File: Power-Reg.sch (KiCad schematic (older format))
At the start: 9 parts, among them U201 MCP6002, U401 TPS7A2401

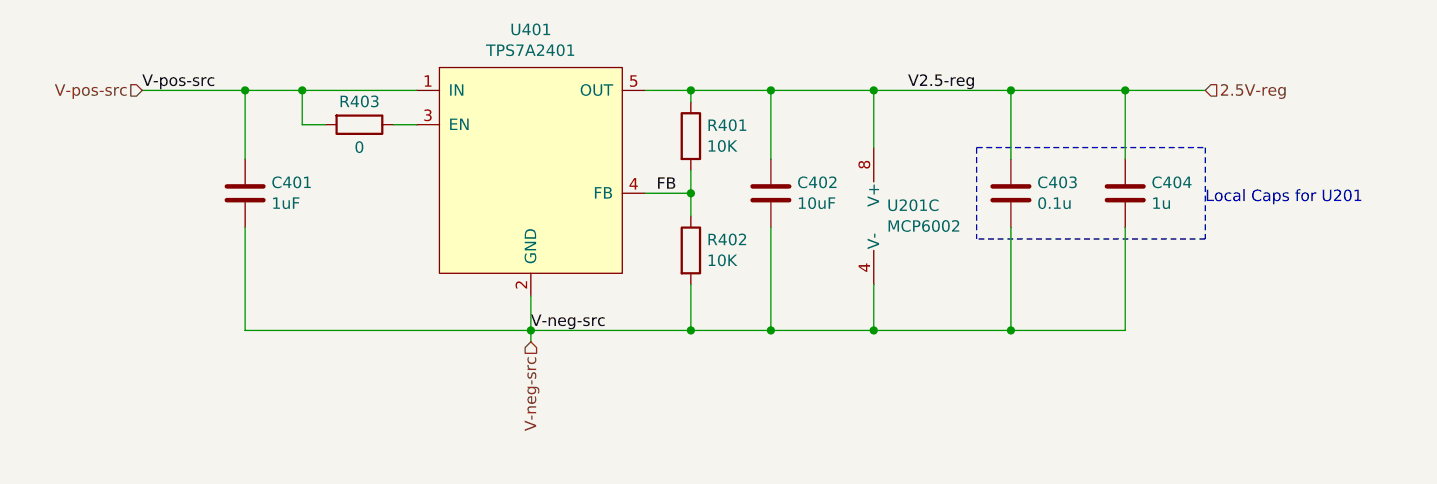
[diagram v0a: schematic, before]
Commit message: PCB completed with Op-Amp mounted horizontally
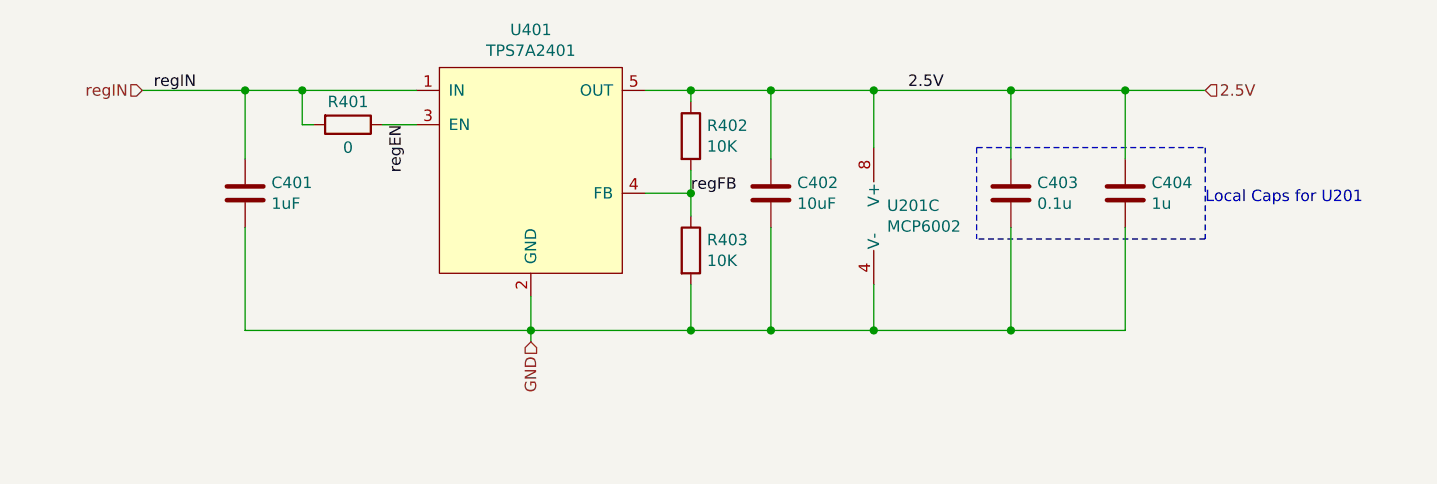
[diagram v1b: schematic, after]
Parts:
- U201: MPN (none) -> MCP6002T-I/SN
- U401: MPN (none) -> TPS7A2401DBVR
- renumbered R403 to R401, R401 to R402, R402 to R403
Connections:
- net regEN: now reaches R401.1, U401.3 (EN)
- net 2.5V-reg renamed 2.5V
- net FB renamed regFB
- net V-neg-src renamed GND
- net V-pos-src renamed regIN
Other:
- moved on the sheet: R401
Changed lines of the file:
@@
 F 2 "Package_SO:SOIC-8_3.9x4.9mm_P1.27mm" H 6950 3800 50  0001 C CNN
 F 3 "http://ww1.microchip.com/downloads/en/DeviceDoc/21733j.pdf" H 6950 3800 50  0001 C CNN
+F 4 "MCP6002T-I/SN" H 6950 3800 50  0001 C CNN "MPN"
 	3    6950 3800
 	1    0    0    -1
@@
 F 1 "TPS7A2401" H 5350 4124 50  0000 C CNN
 F 2 "Package_TO_SOT_SMD:SOT-23-5_HandSoldering" H 5350 3600 50  0001 C CNN
-F 3 "" H 5350 3600 50  0001 C CNN
+F 3 "https://www.ti.com/lit/ds/symlink/tps7a24.pdf?HQS=dis-dk-null-digikeymode-dsf-pf-null-wwe&ts=1613174744075" H 5350 3600 50  0001 C CNN
+F 4 "TPS7A2401DBVR" H 5350 3600 50  0001 C CNN "MPN"
 	1    5350 3600
 	1    0    0    -1
@@
 P 6050 3450
 AR Path="/60164E14" Ref="R?"  Part="1"
-AR Path="/601B7636/60164E14" Ref="R401"  Part="1"
-F 0 "R401" H 6120 3496 50  0000 L CNN
+AR Path="/601B7636/60164E14" Ref="R402"  Part="1"
+F 0 "R402" H 6120 3496 50  0000 L CNN
 F 1 "10K" H 6120 3405 50  0000 L CNN
 F 2 "Resistor_SMD:R_0805_2012Metric_Pad1.20x1.40mm_HandSolder" V 5980 3450 50  0001 C CNN
@@
 P 6050 3950
 AR Path="/60164E1A" Ref="R?"  Part="1"
-AR Path="/601B7636/60164E1A" Ref="R402"  Part="1"
-F 0 "R402" H 6120 3996 50  0000 L CNN
+AR Path="/601B7636/60164E1A" Ref="R403"  Part="1"
+F 0 "R403" H 6120 3996 50  0000 L CNN
 F 1 "10K" H 6120 3905 50  0000 L CNN
 F 2 "Resistor_SMD:R_0805_2012Metric_Pad1.20x1.40mm_HandSolder" V 5980 3950 50  0001 C CNN
@@
 	6400 4300 6050 4300
 Text HLabel 8300 3250 2    50   Input ~ 0
-2.5V-reg
+2.5V
 Wire Wire Line
 	4100 3250 3650 3250
 Connection ~ 4100 3250
-Text HLabel 5350 4350 3    50   Input ~ 0
-V-neg-src
 Text HLabel 3650 3250 0    50   Input ~ 0
-V-pos-src
-Text Label 5900 3700 0    50   ~ 0
-FB
-Text Label 3650 3250 0    50   ~ 0
-V-pos-src
-Text Label 5350 4300 0    50   ~ 0
-V-neg-src
+regIN
+Text Label 6050 3700 0    50   ~ 0
+regFB
+Text Label 3700 3250 0    50   ~ 0
+regIN
 Text Label 7000 3250 0    50   ~ 0
-V2.5-reg
+2.5V
 Wire Wire Line
 	4100 3250 4350 3250
 $Comp
-L Device:R R403
+L Device:R R401
 U 1 1 601B0CA0
-P 4600 3400
-F 0 "R403" V 4500 3400 50  0000 C CNN
-F 1 "0" V 4700 3400 50  0000 C CNN
-F 2 "Resistor_SMD:R_0805_2012Metric_Pad1.20x1.40mm_HandSolder" V 4530 3400 50  0001 C CNN
-F 3 "~" H 4600 3400 50  0001 C CNN
-	1    4600 3400
+P 4550 3400
+F 0 "R401" V 4450 3400 50  0000 C CNN
+F 1 "0" V 4650 3400 50  0000 C CNN
+F 2 "Resistor_SMD:R_0805_2012Metric_Pad1.20x1.40mm_HandSolder" V 4480 3400 50  0001 C CNN
+F 3 "~" H 4550 3400 50  0001 C CNN
+	1    4550 3400
 	0    1    1    0
 $EndComp
 Wire Wire Line
-	4750 3400 4850 3400
-Wire Wire Line
-	4450 3400 4350 3400
+	4700 3400 4850 3400
+Wire Wire Line
+	4400 3400 4350 3400
 Wire Wire Line
 	4350 3400 4350 3250
@@
 Text Notes 8300 3750 0    50   ~ 0
 Local Caps for U201
+Text HLabel 5350 4350 3    50   Input ~ 0
+GND
+Text Label 4800 3400 3    50   ~ 0
+regEN
 $EndSCHEMATC

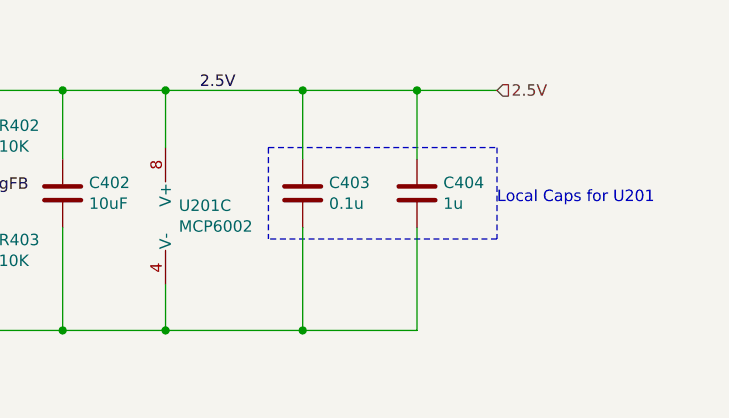
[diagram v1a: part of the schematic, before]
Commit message: Revision A as sent to OSHPark with some MPN updates due to availability
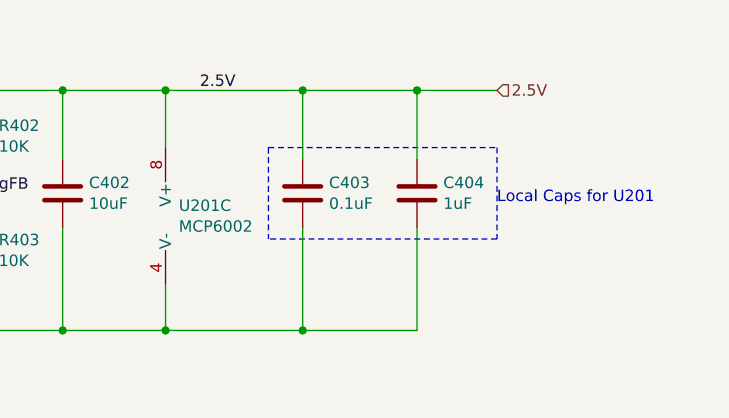
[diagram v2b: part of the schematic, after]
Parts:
- C403: value 0.1u -> 0.1uF
- C404: value 1u -> 1uF
- R401, R402, R403: footprint Resistor_SMD:R_0805_2012Metric_Pad1.20x1.40mm_HandSolder -> Resistor_SMD:R_0603_1608Metric_Pad0.98x0.95mm_HandSolder
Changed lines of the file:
@@
 F 0 "R402" H 6120 3496 50  0000 L CNN
 F 1 "10K" H 6120 3405 50  0000 L CNN
-F 2 "Resistor_SMD:R_0805_2012Metric_Pad1.20x1.40mm_HandSolder" V 5980 3450 50  0001 C CNN
+F 2 "Resistor_SMD:R_0603_1608Metric_Pad0.98x0.95mm_HandSolder" V 5980 3450 50  0001 C CNN
 F 3 "~" H 6050 3450 50  0001 C CNN
 	1    6050 3450
@@
 F 0 "R403" H 6120 3996 50  0000 L CNN
 F 1 "10K" H 6120 3905 50  0000 L CNN
-F 2 "Resistor_SMD:R_0805_2012Metric_Pad1.20x1.40mm_HandSolder" V 5980 3950 50  0001 C CNN
+F 2 "Resistor_SMD:R_0603_1608Metric_Pad0.98x0.95mm_HandSolder" V 5980 3950 50  0001 C CNN
 F 3 "~" H 6050 3950 50  0001 C CNN
 	1    6050 3950
@@
 F 0 "R401" V 4450 3400 50  0000 C CNN
 F 1 "0" V 4650 3400 50  0000 C CNN
-F 2 "Resistor_SMD:R_0805_2012Metric_Pad1.20x1.40mm_HandSolder" V 4480 3400 50  0001 C CNN
+F 2 "Resistor_SMD:R_0603_1608Metric_Pad0.98x0.95mm_HandSolder" V 4480 3400 50  0001 C CNN
 F 3 "~" H 4550 3400 50  0001 C CNN
 	1    4550 3400
@@
 P 7450 3700
 F 0 "C403" H 7565 3746 50  0000 L CNN
-F 1 "0.1u" H 7565 3655 50  0000 L CNN
+F 1 "0.1uF" H 7565 3655 50  0000 L CNN
 F 2 "Capacitor_SMD:C_0603_1608Metric_Pad1.08x0.95mm_HandSolder" H 7488 3550 50  0001 C CNN
 F 3 "~" H 7450 3700 50  0001 C CNN
@@
 P 7950 3700
 F 0 "C404" H 8065 3746 50  0000 L CNN
-F 1 "1u" H 8065 3655 50  0000 L CNN
+F 1 "1uF" H 8065 3655 50  0000 L CNN
 F 2 "Capacitor_SMD:C_0603_1608Metric_Pad1.08x0.95mm_HandSolder" H 7988 3550 50  0001 C CNN
 F 3 "~" H 7950 3700 50  0001 C CNN

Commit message: Revision 1 release
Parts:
- C402: MPN (none) -> CL10A106MQ8NNNC
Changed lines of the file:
@@
 F 2 "Capacitor_SMD:C_0603_1608Metric_Pad1.08x0.95mm_HandSolder" H 6438 3550 50  0001 C CNN
 F 3 "~" H 6400 3700 50  0001 C CNN
+F 4 "CL10A106MQ8NNNC" H 6400 3700 50  0001 C CNN "MPN"
 	1    6400 3700
 	1    0    0    -1
